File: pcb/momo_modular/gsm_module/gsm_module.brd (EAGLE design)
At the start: 50.8 x 33 mm, 20 parts, among them U1 PIC16LF1823, U2 TI-HIGHSIDE-PFET, U3 SIM900

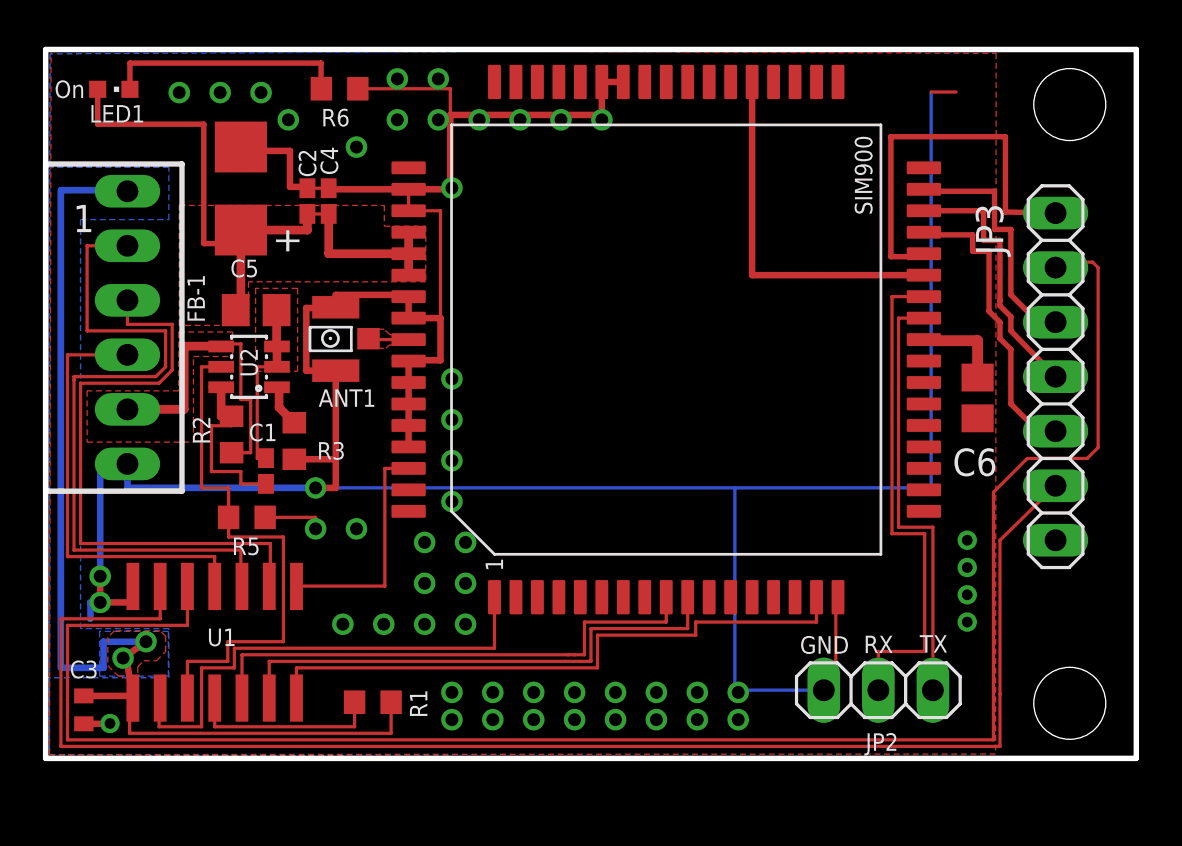
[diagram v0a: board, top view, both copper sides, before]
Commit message: Make GSM board fit into 1.3x2" board.
- Removes need for separate Card Adapter board
- GSM module now has integrated SIM Card holder
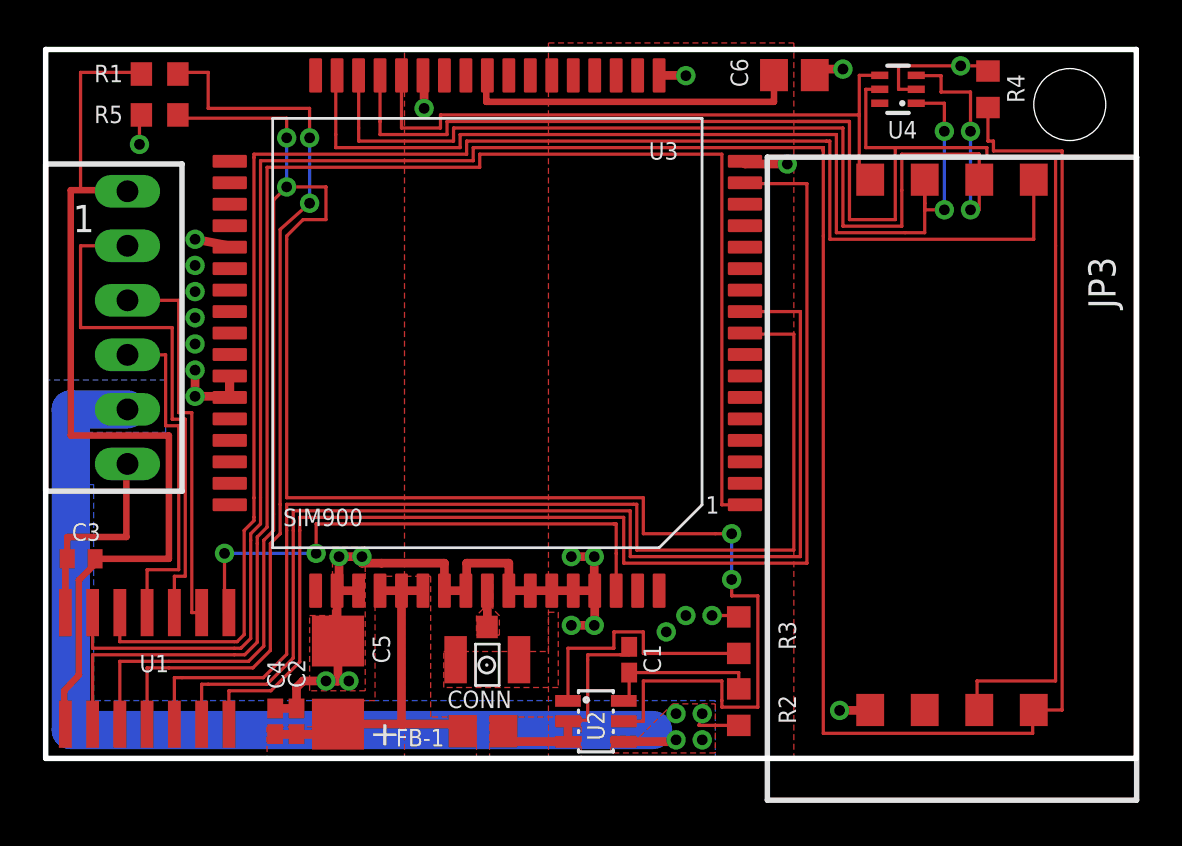
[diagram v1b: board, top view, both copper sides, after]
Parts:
- removed ANT1: RFANTENNA, components:RFJACK
- removed JP2: (no value), pinhead:1X03
- removed LED1: (no value), led:CHIPLED_0603
- removed R6: 470R, rcl:R0603
- added CONN: RFANTENNA, components:RFJACK
- added R4: 10K, rcl:R0603
- added U4: ESD-SMF05C, components:SC70-6L
- JP3: value (none) -> SIMHOLDER-8PINHING; device pinhead:1X07 -> components:CCM03-SIMHOLDER
- moved R1 30.9 mm to (10.4, 37.0), turned to 180 degrees
- moved R2 26.8 mm to (37.4, 7.47)
- moved C4 24.4 mm to (15.8, 6.81)
- moved C2 24.2 mm to (16.8, 6.81)
- moved C5 23.5 mm to (18.7, 8.61)
- moved U2 23.1 mm to (30.7, 6.81), turned to 270 degrees
- moved R3 22.6 mm to (37.4, 10.8), turned to 270 degrees
- moved FB-1 22.3 mm to (25.5, 6.35)
- moved R5 19.2 mm to (10.4, 35.1), turned to 0 degrees
- moved C1 19.1 mm to (32.3, 9.68)
- moved C6 17.3 mm to (40.0, 36.9), turned to 0 degrees
- moved U3 8.34 mm to (25.7, 24.9), turned to 180 degrees
- moved C3 7.04 mm to (6.73, 14.4), turned to 180 degrees
- moved JP3 5.78 mm to (47.3, 19.7), turned to 90 degrees
- moved U1 3.38 mm to (9.80, 9.27)
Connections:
- removed net DEBUGRX: JP2.2, U3.28
- removed net DEBUGTX: JP2.1, U3.27
- removed net N$2: LED1.C, R6.2
- net GND: now also CONN.UNUSED1, CONN.UNUSED2, JP3.GND, R4.1, U4.2; no longer ANT1.UNUSED1, ANT1.UNUSED2, JP2.3, JP3.7, R6.1
- net N$7: now also CONN.ANTENNA; no longer ANT1.ANTENNA
- net SIMCLK: now also JP3.CLOCK, U4.3; no longer JP3.4
- net SIMDAT: now also JP3.IO, U4.5; no longer JP3.5
- net SIMRST: now also JP3.RESET, U4.1; no longer JP3.3
- net SIMVCC: now also JP3.VCC, U4.4; no longer JP3.1
- net SW1: now also JP3.SW1; no longer JP3.2
- net SW2: now also JP3.SW2, R4.2; no longer JP3.6
- net VDD: no longer LED1.A
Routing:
- net GND: track 174.9 -> 66.6 mm, vias 52 -> 25
- net POW-SW-ON: track 24.6 -> 98.9 mm, vias 0 -> 4
- net SIMDAT: track 14.0 -> 79.9 mm
- net SW2: track 69.0 -> 129.6 mm
- net PWRKEY: track 23.0 -> 72.7 mm
- net SIMCLK: track 12.3 -> 52.7 mm, vias 0 -> 2
- net SIMRST: track 11.6 -> 47.2 mm, vias 0 -> 2
- net V+: track 14.8 -> 49.6 mm, vias 0 -> 4
- net N$6: track 9.34 -> 42.6 mm, vias 0 -> 2
- net RESET: track 28.9 -> 58.5 mm
- net RXD: track 24.2 -> 53.2 mm
- net TXD: track 24.5 -> 53.0 mm
- net DEBUGRX: track 23.5 -> 0.00 mm
- net DEBUGTX: track 20.1 -> 0.00 mm
- net STATUS: track 10.7 -> 25.7 mm, vias 0 -> 2
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- added copper zone on layer 16, net V+
- removed copper zone on layer 1, net VCCINT
- removed copper zone on layer 16, net VCCINT
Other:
- board text removed: "GND"
- board text removed: "On"
- board text removed: "RX"
- board text removed: "TX"
